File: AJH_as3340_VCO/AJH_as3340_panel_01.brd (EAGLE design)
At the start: 30 x 128.5 mm, 1 part

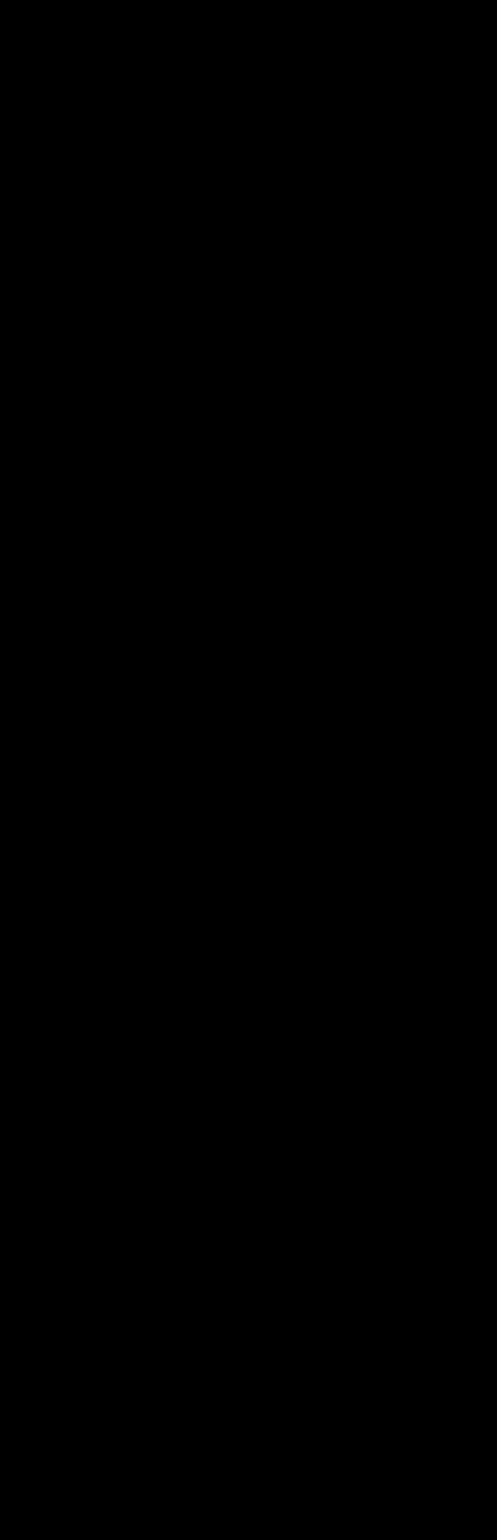
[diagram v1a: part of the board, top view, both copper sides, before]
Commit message: Fixed FP objects
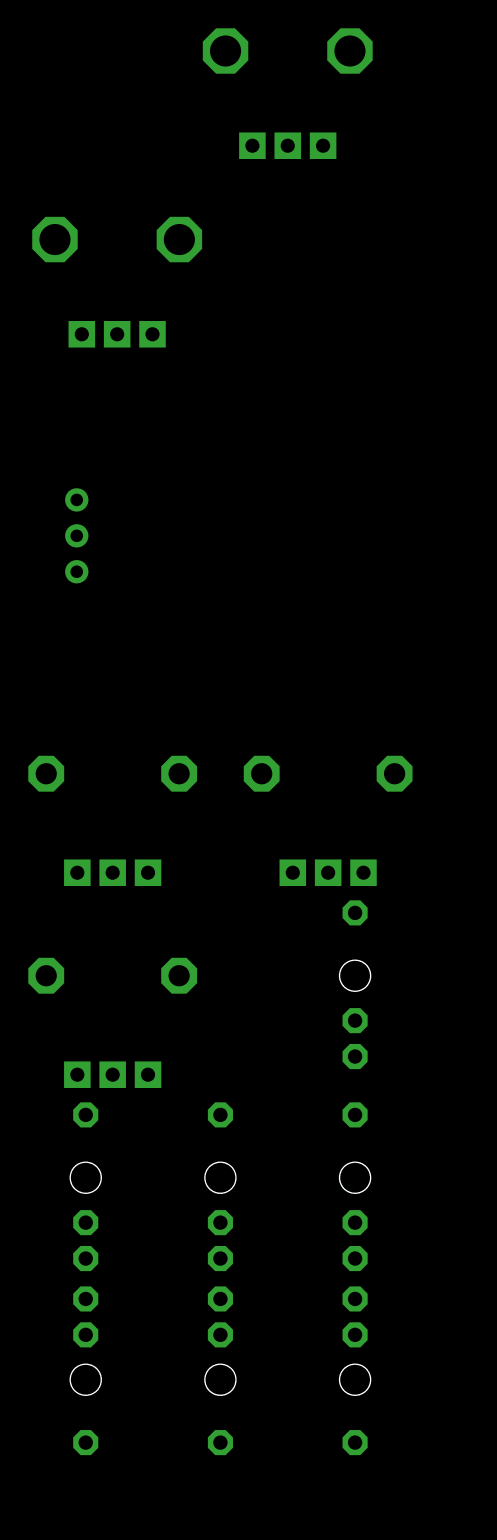
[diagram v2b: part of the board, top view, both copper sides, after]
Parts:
- added FM_IN1, PWM_IN1, P_OUT1, SYNC_IN1, S_OUT1, T_OUT1, V_OCT1: PJ301_THONKICONN6, og-pj301_variations:WQP_PJ_301M6
- added FM_MOD1, PW1, PWM1: 10kB, pot-alps:ALPS_POT_VERTICAL_PS
- added OSC_COARSE1, OSC_FINE1: 10kB, og-pots:ALPS_POT_VERTICAL
- added SYNC_SW1: submini-3T, malekko main:SPDT-SUB
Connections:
- new net -5V1: OSC_COARSE1.P$3, OSC_FINE1.P$3
- new net 5V1: OSC_COARSE1.P$1, OSC_FINE1.P$1, PW1.P$1
- new net GND1: FM_IN1.P1, FM_IN1.P2, PW1.P$3, PWM1.P$3, PWM_IN1.P1, PWM_IN1.P2, P_OUT1.P1, SYNC_IN1.P1, SYNC_IN1.P2, S_OUT1.P1, T_OUT1.P1, V_OCT1.P1, V_OCT1.P2
- new net HARDSYNC_IN1: SYNC_SW1.P$1
- new net MAIN_CV2: PWM1.P$1, PWM_IN1.P3
- new net N$13: PW1.P$2
- new net N$14: FM_MOD1.P$2
- new net N$15: P_OUT1.P3
- new net N$16: T_OUT1.P3
- new net N$2: PWM1.P$2
- new net N$5: FM_IN1.P3, FM_MOD1.P$1
- new net N$6: S_OUT1.P3
- new net N$7: OSC_FINE1.P$2
- new net N$8: OSC_COARSE1.P$2
- new net N$9: V_OCT1.P3
- new net SOFTSYNC_IN1: SYNC_SW1.P$3
- new net SYNC_IN1: SYNC_IN1.P3, SYNC_SW1.P$2

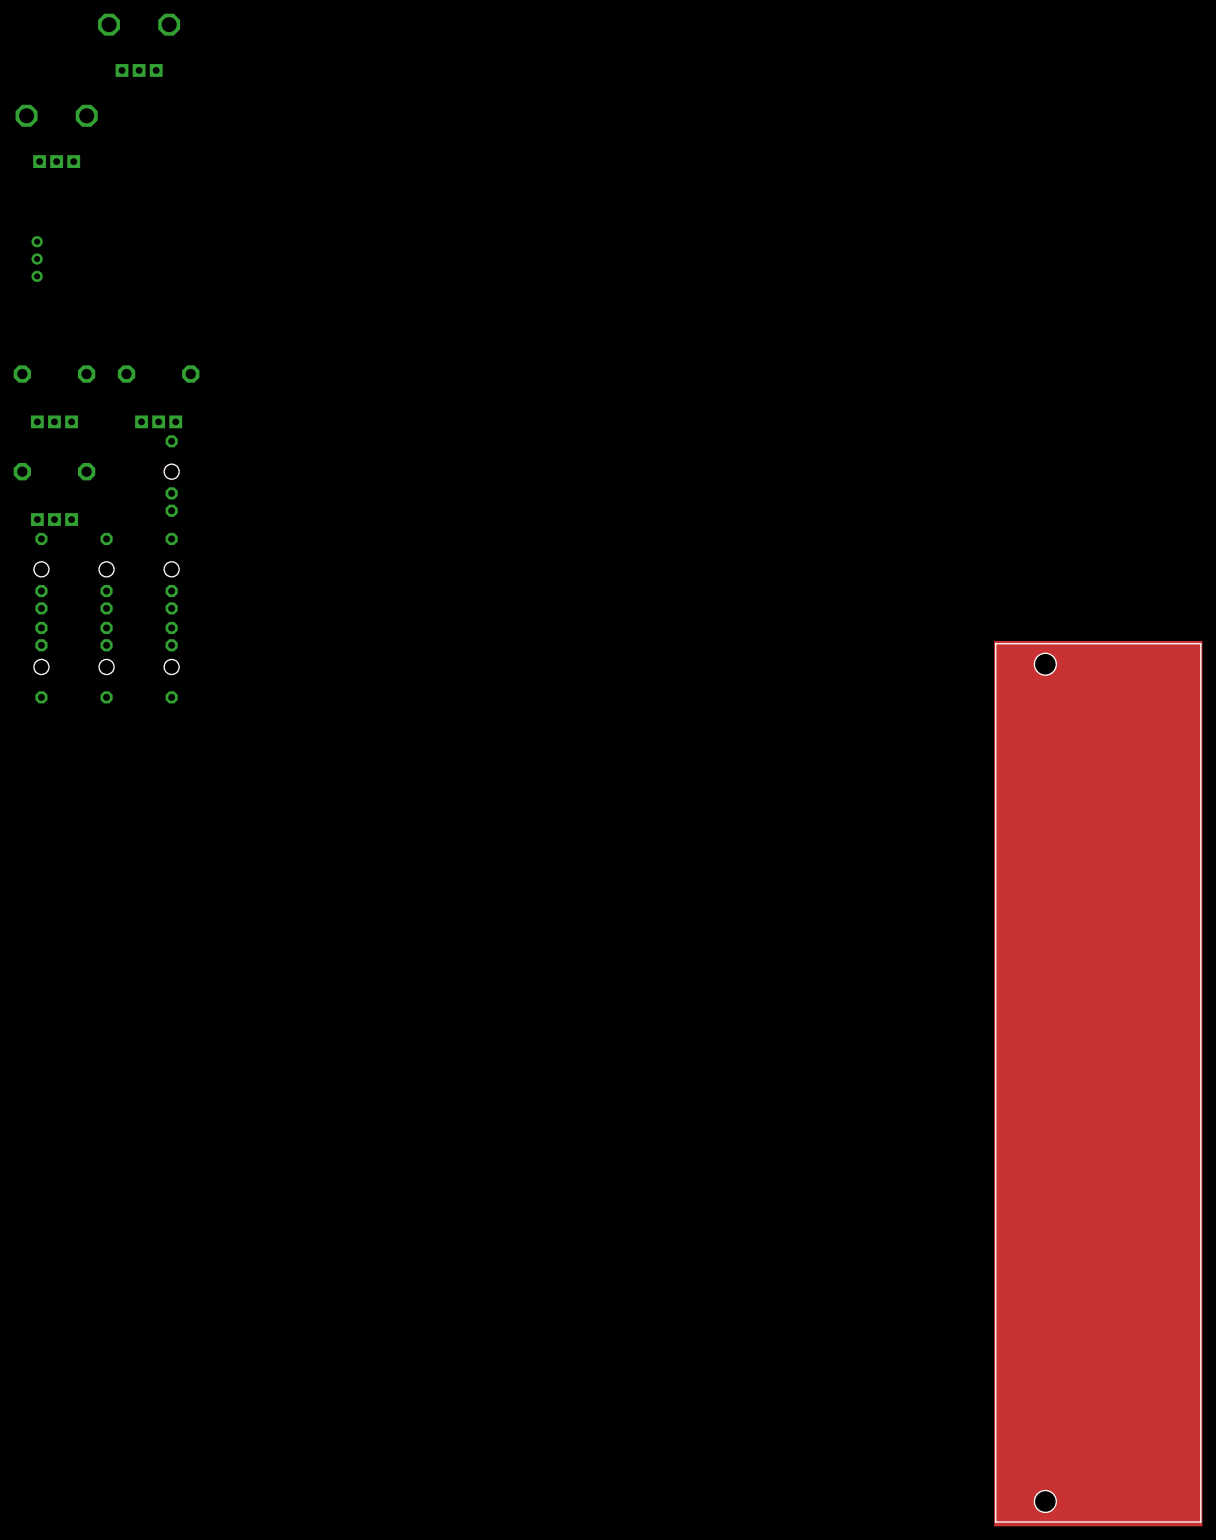
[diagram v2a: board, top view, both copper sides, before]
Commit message: Mirrored holes to FP
UI DESIGN FREEZE!!
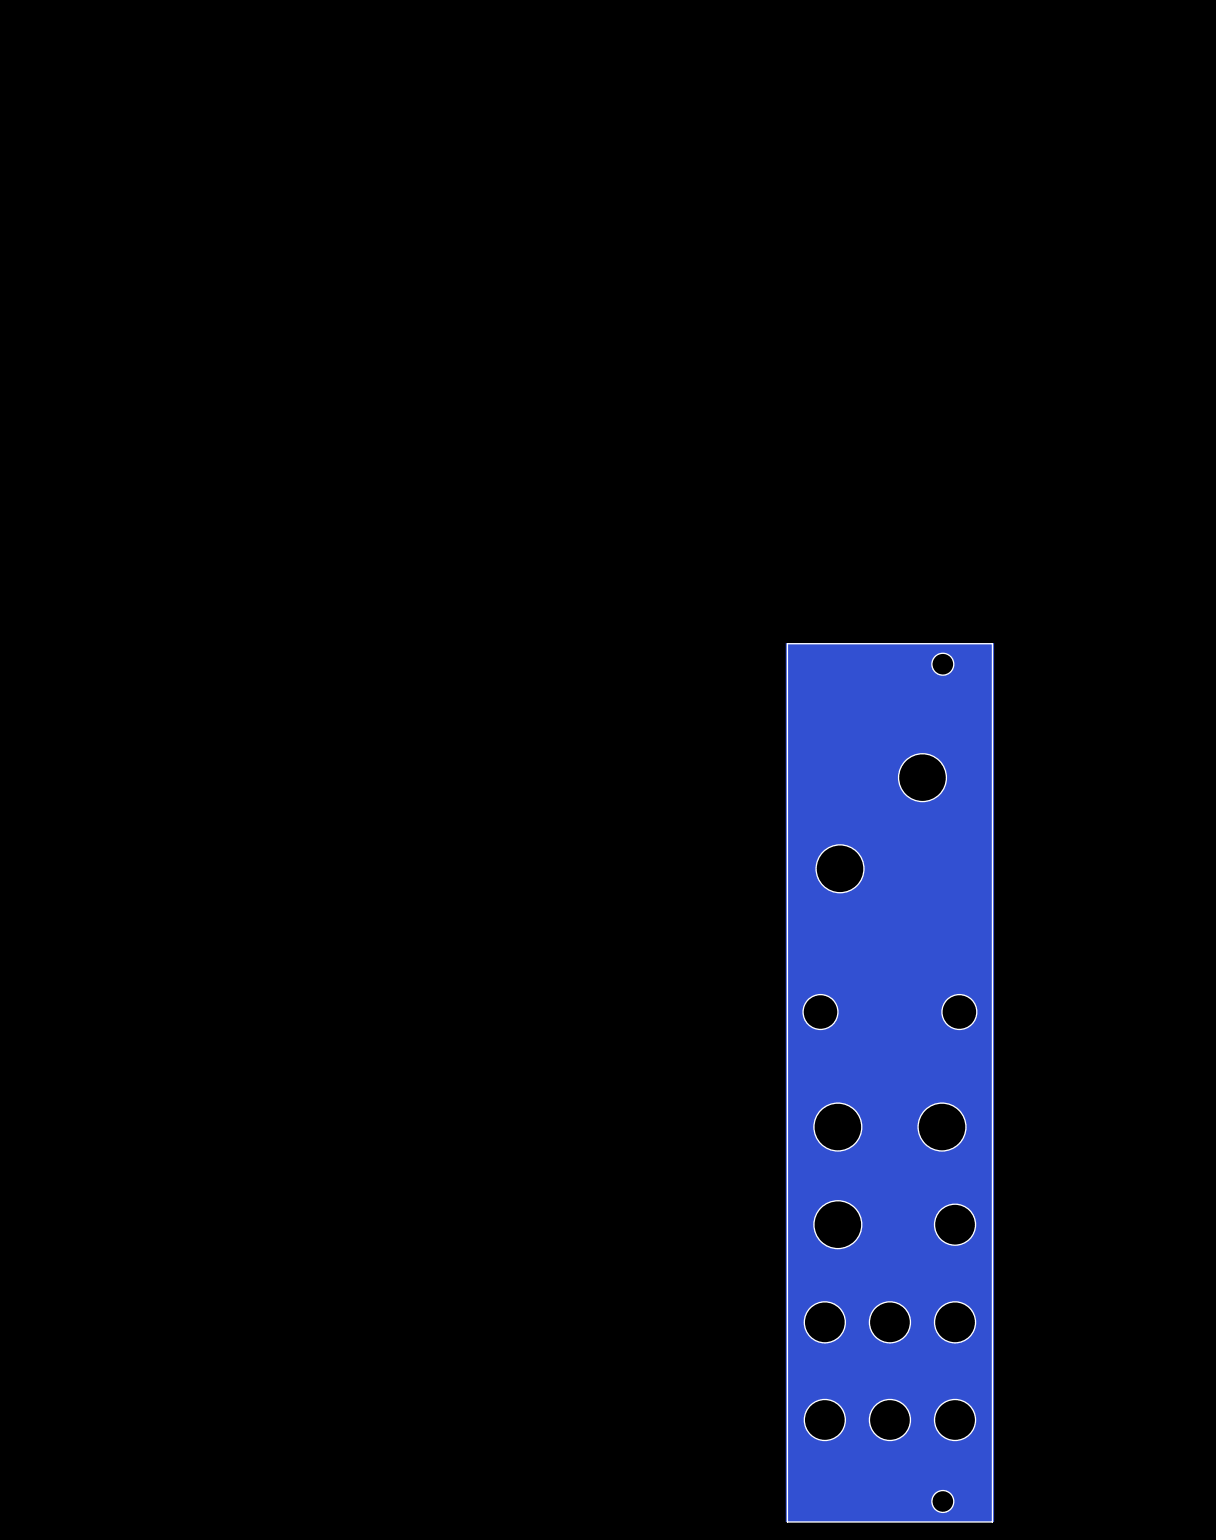
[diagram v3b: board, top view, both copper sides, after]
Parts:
- removed FM_IN1, PWM_IN1, P_OUT1, SYNC_IN1, S_OUT1, T_OUT1, V_OCT1: PJ301_THONKICONN6, og-pj301_variations:WQP_PJ_301M6
- removed FM_MOD1, PW1, PWM1: 10kB, pot-alps:ALPS_POT_VERTICAL_PS
- removed OSC_COARSE1, OSC_FINE1: 10kB, og-pots:ALPS_POT_VERTICAL
- removed SYNC_SW1: submini-3T, malekko main:SPDT-SUB
- flipped E$1 to the bottom
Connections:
- removed net -5V1: OSC_COARSE1.P$3, OSC_FINE1.P$3
- removed net 5V1: OSC_COARSE1.P$1, OSC_FINE1.P$1, PW1.P$1
- removed net GND1: FM_IN1.P1, FM_IN1.P2, PW1.P$3, PWM1.P$3, PWM_IN1.P1, PWM_IN1.P2, P_OUT1.P1, SYNC_IN1.P1, SYNC_IN1.P2, S_OUT1.P1, T_OUT1.P1, V_OCT1.P1, V_OCT1.P2
- removed net HARDSYNC_IN1: SYNC_SW1.P$1
- removed net MAIN_CV2: PWM1.P$1, PWM_IN1.P3
- removed net N$13: PW1.P$2
- removed net N$14: FM_MOD1.P$2
- removed net N$15: P_OUT1.P3
- removed net N$16: T_OUT1.P3
- removed net N$2: PWM1.P$2
- removed net N$5: FM_IN1.P3, FM_MOD1.P$1
- removed net N$6: S_OUT1.P3
- removed net N$7: OSC_FINE1.P$2
- removed net N$8: OSC_COARSE1.P$2
- removed net N$9: V_OCT1.P3
- removed net SOFTSYNC_IN1: SYNC_SW1.P$3
- removed net SYNC_IN1: SYNC_IN1.P3, SYNC_SW1.P$2
